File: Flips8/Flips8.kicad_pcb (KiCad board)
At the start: 2 copper layers, 100 x 100 mm, 24 parts, among them CN1 Conn_02x32_Row_Letter_First_A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, CN2 Conn_02x05_Odd_Even, U1 NCV7708, U2 NCV7708, U3 NCV7708, U4 NCV7708, U5 NCV7708, U6 NCV7708, U7 NCV7708, U8 74LS138

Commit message: proceed with Flips8
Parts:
- moved R1 5.08 mm to (83.8, 146.7), turned to 270 degrees
- moved R3 2.54 mm to (78.7, 146.7), turned to 270 degrees
- moved R2 2.54 mm to (81.3, 146.7), turned to 270 degrees
- moved C3 1.42 mm to (72.4, 127.6), turned to 90 degrees
- moved C2 1.42 mm to (63.5, 107.3), turned to 90 degrees
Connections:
- U3 pad 1: /X1 -> Net-(U3-Pad1)
- U3 pad 2: /X1 -> Net-(U3-Pad2)
- U3 pad 27: Net-(U3-Pad27) -> /X1
- U3 pad 28: Net-(U3-Pad28) -> /X1
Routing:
- net VCC: track 19.0 -> 142.4 mm, vias 1 -> 5
- net /X8: track 0.00 -> 92.7 mm
- net /X1: track 1.27 -> 92.0 mm
- net /X7: track 0.00 -> 87.6 mm
- net /X2: track 0.00 -> 87.4 mm
- net /X9: track 0.00 -> 81.3 mm
- net /X5: track 0.00 -> 80.4 mm
- net /X4: track 0.00 -> 77.2 mm
- net /X6: track 0.00 -> 76.8 mm
- net /X10: track 0.00 -> 76.8 mm
- net /X3: track 0.00 -> 74.7 mm
- net /SO: track 19.8 -> 94.5 mm, vias 1 -> 4
- net /EN: track 21.4 -> 95.8 mm, vias 1 -> 4
- net /~SY12: track 0.00 -> 73.3 mm
- net /X14: track 0.00 -> 69.5 mm
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
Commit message: finish initial routing of Flips8
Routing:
- net /SI: track 76.9 -> 282.1 mm, vias 3 -> 8
- net /SCLK: track 77.5 -> 280.7 mm, vias 3 -> 8
- net /SO: track 94.5 -> 294.0 mm, vias 4 -> 9
- net /EN: track 95.8 -> 286.3 mm, vias 4 -> 9
- net VCC: track 142.4 -> 281.4 mm, vias 5 -> 9
- net /~CS7: track 0.00 -> 133.0 mm, vias 0 -> 2
- net /~CS6: track 0.00 -> 117.4 mm, vias 0 -> 2
- net +12V: track 133.5 -> 240.8 mm, vias 6 -> 10
- net /~CS5: track 0.00 -> 101.1 mm, vias 0 -> 2
- net /~CS4: track 0.00 -> 38.6 mm, vias 0 -> 2
- net /~CS1: track 62.1 -> 61.0 mm
- net /~CS2: track 50.3 -> 49.5 mm
- net /CSA2: track 31.0 -> 30.3 mm

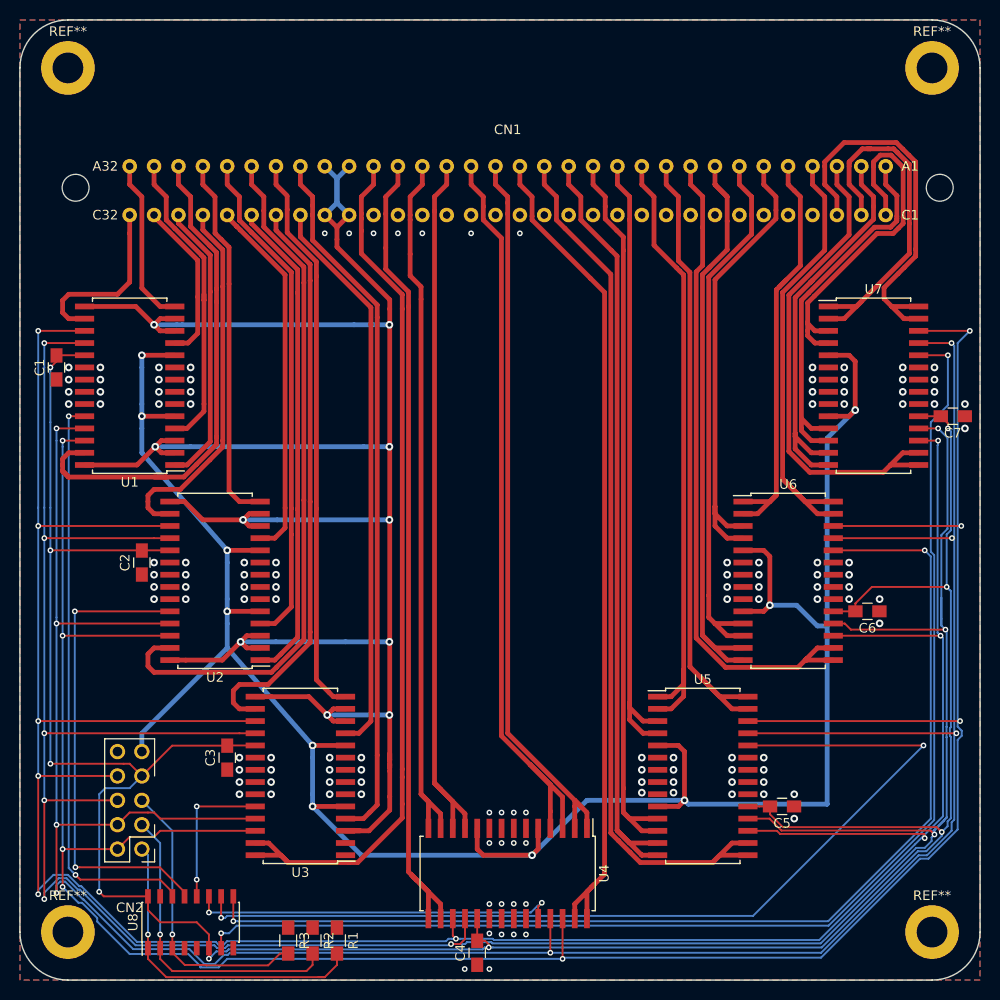
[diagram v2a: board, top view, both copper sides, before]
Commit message: more systematic tracing for Flisp8
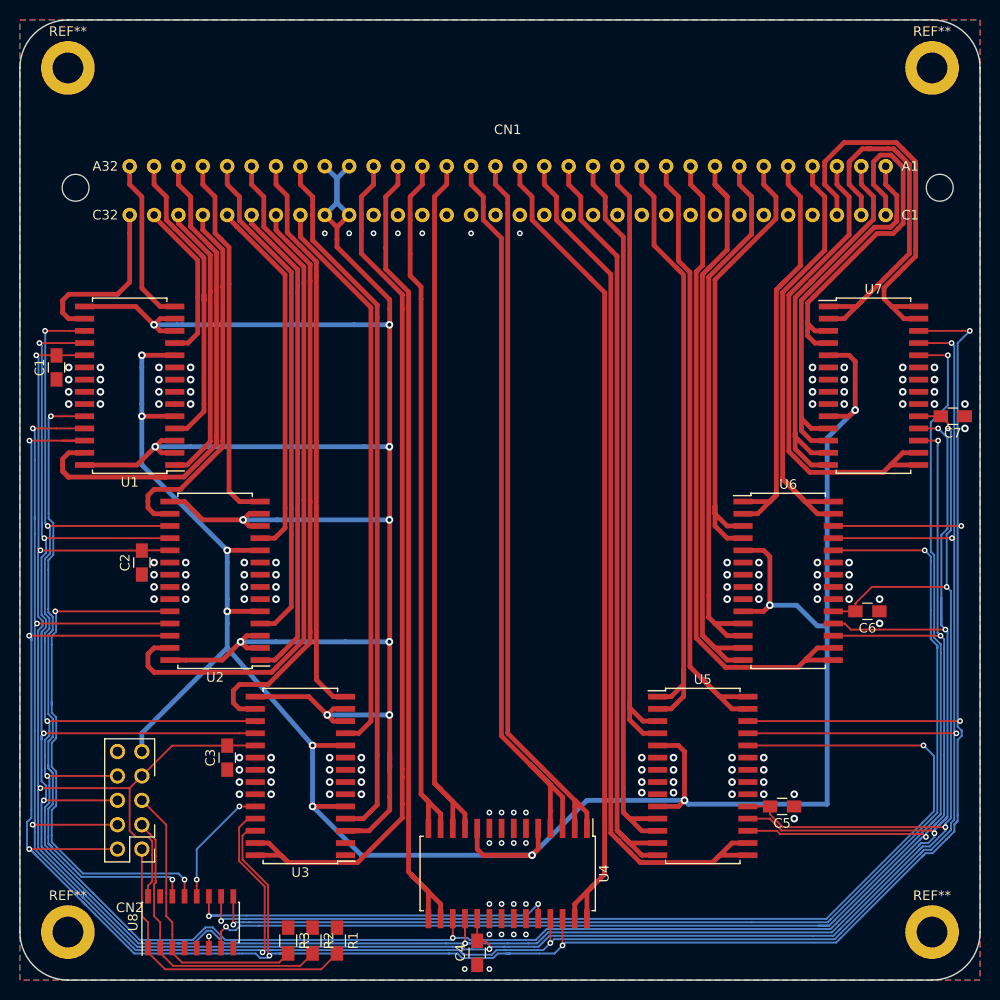
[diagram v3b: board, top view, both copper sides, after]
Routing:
- net VCC: track 281.4 -> 302.4 mm, vias 9 -> 8
- net /SI: track 282.1 -> 298.5 mm
- net /SCLK: track 280.7 -> 287.3 mm
- net /~CS1: track 61.0 -> 67.2 mm
- net /~CS5: track 101.1 -> 107.1 mm
- net /~CS2: track 49.5 -> 54.5 mm
- net /~CS7: track 133.0 -> 137.1 mm
- net /EN: track 286.3 -> 283.6 mm, vias 9 -> 8
- net /~CS3: track 15.5 -> 12.9 mm
- net /CSA0: track 34.5 -> 32.1 mm, vias 1 -> 0
- net /CSA1: track 32.6 -> 31.2 mm, vias 1 -> 0
- net /~CS6: track 117.4 -> 118.7 mm
- net /SO: track 294.0 -> 293.2 mm, vias 9 -> 8
- net /~CS4: track 38.6 -> 39.2 mm
- net /CSA2: track 30.3 -> 30.1 mm, vias 1 -> 0

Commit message: reposition ncv7708 of Flisp8
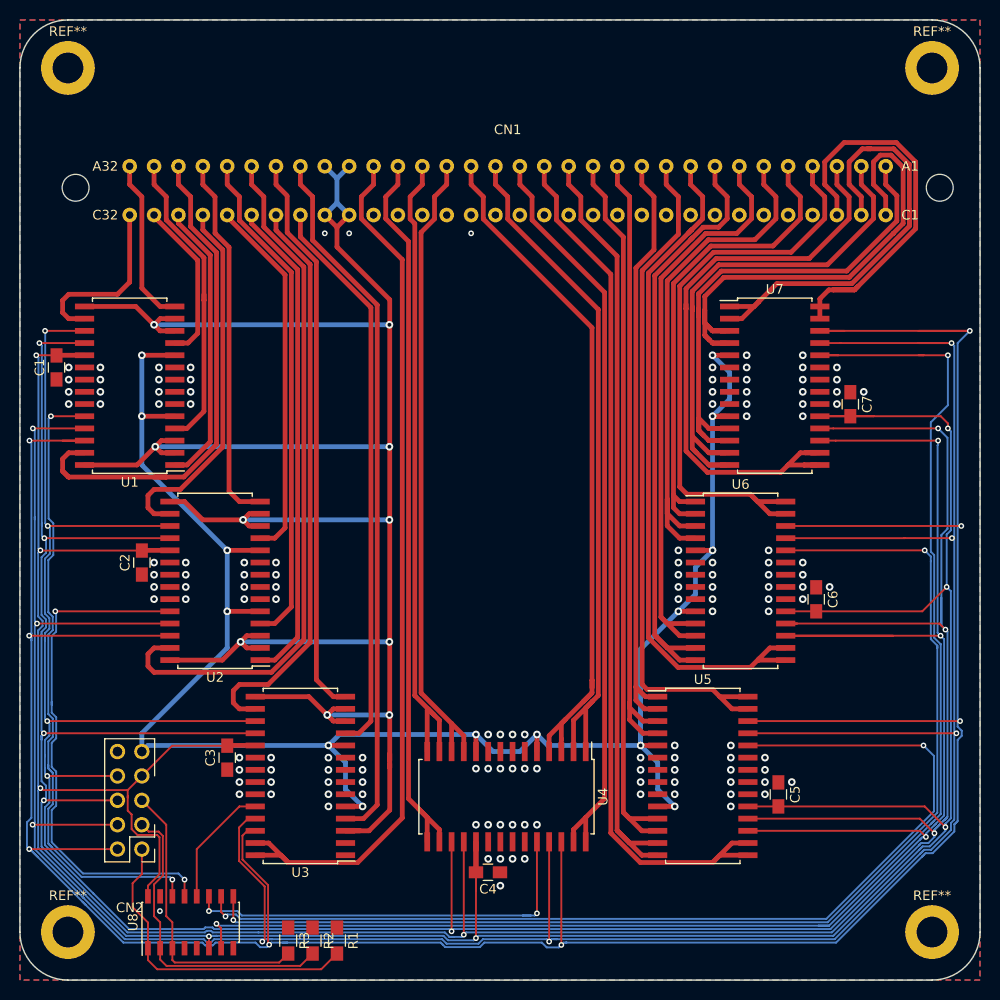
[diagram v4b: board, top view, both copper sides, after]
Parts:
- moved C7 10.7 mm to (137.3, 90.8), turned to 270 degrees
- moved U7 10.3 mm to (129.4, 88.9)
- moved C4 8.46 mm to (99.5, 139.6), turned to 180 degrees
- moved U4 8.00 mm to (101.5, 131.7)
- moved C6 5.48 mm to (133.7, 111.1), turned to 270 degrees
- moved U6 4.95 mm to (125.9, 109.2)
- moved C5 1.31 mm to (129.8, 131.5), turned to 270 degrees
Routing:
- net +12V: track 241.2 -> 202.0 mm, vias 10 -> 14
- net VCC: track 302.4 -> 334.5 mm
- net /EN: track 283.6 -> 313.1 mm
- net /SI: track 298.5 -> 327.5 mm
- net /SCLK: track 287.3 -> 312.5 mm
- net /SO: track 293.2 -> 314.6 mm
- net /X22: track 39.6 -> 57.7 mm
- net /X23: track 37.7 -> 55.4 mm
- net /X21: track 42.3 -> 57.9 mm
- net /X20: track 51.0 -> 64.8 mm
- net /X19: track 47.9 -> 61.1 mm
- net /~CS7: track 137.1 -> 150.0 mm
- net /X2: track 87.4 -> 77.0 mm
- net /X4: track 77.2 -> 66.8 mm
- net /X7: track 87.6 -> 77.9 mm
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
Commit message: more cleanup on pcb
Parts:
- moved U1 6.86 mm to (69.1, 88.9)
- moved C1 6.60 mm to (61.2, 87.1)
- moved U2 4.83 mm to (75.9, 109.2)
- moved C2 4.57 mm to (68.1, 107.3)
- moved C3 0.25 mm to (72.1, 127.6)
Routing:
- net /RY: track 234.1 -> 202.6 mm
- net /SCLK: track 312.5 -> 331.6 mm
- net /SO: track 314.6 -> 330.4 mm
- net /EN: track 313.1 -> 324.9 mm
- net VCC: track 334.5 -> 345.9 mm
- net /~SY13: track 59.9 -> 71.2 mm
- net /~SY7: track 38.7 -> 49.6 mm
- net /X23: track 55.4 -> 46.3 mm
- net /X22: track 57.7 -> 49.5 mm
- net +12V: track 202.0 -> 193.9 mm
- net /X21: track 57.9 -> 50.1 mm
- net /~CS1: track 67.2 -> 74.8 mm
- net /SI: track 327.5 -> 334.5 mm
- net /~SY1: track 18.6 -> 12.4 mm
- net /~CS2: track 54.5 -> 60.1 mm
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
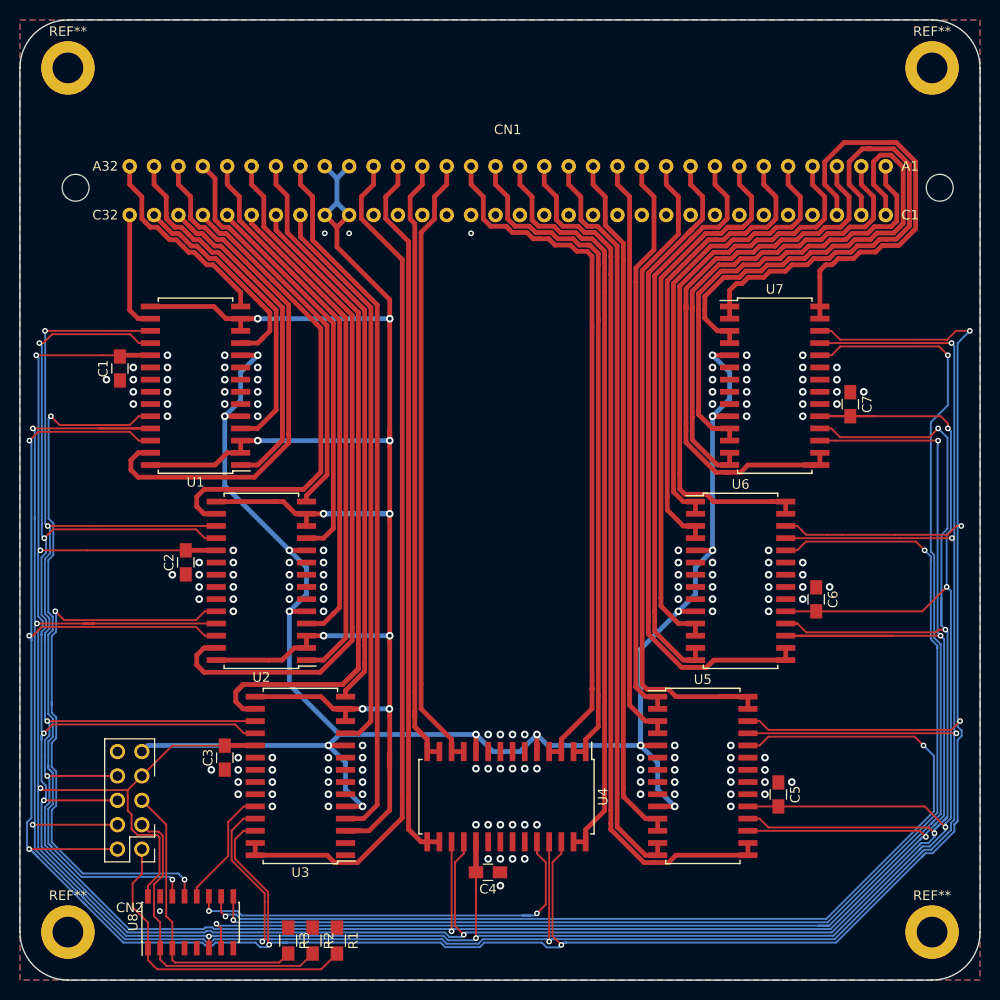
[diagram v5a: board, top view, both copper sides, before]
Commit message: rearrange connector and decoder; move 'bus' away from board edge pt. 1
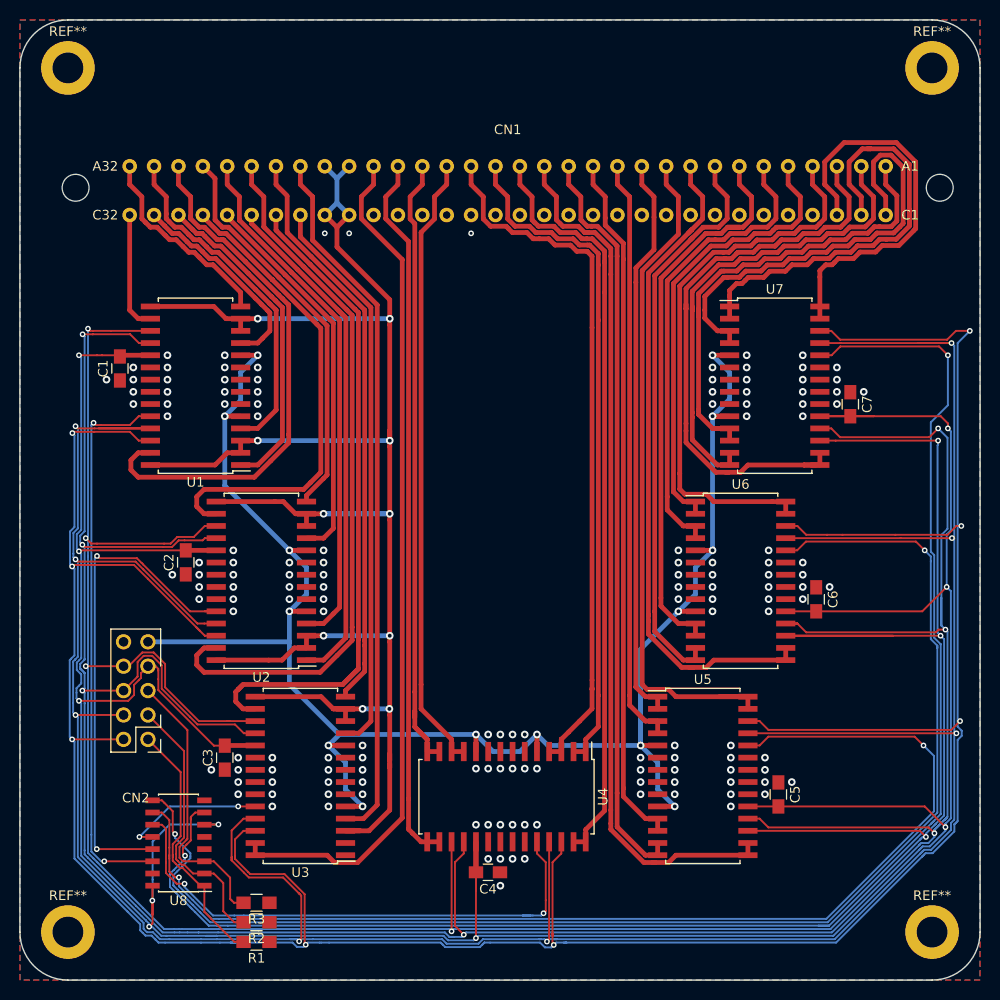
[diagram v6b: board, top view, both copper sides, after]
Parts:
- moved CN2 11.4 mm to (64.1, 125.7)
- moved R1 8.38 mm to (75.4, 146.8), turned to 180 degrees
- moved U8 8.35 mm to (67.3, 136.5), turned to 180 degrees
- moved R2 6.14 mm to (75.4, 144.8), turned to 180 degrees
- moved R3 5.14 mm to (75.4, 142.7), turned to 180 degrees
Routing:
- net /EN: track 324.9 -> 304.1 mm, vias 8 -> 7
- net /SO: track 330.4 -> 311.9 mm, vias 8 -> 7
- net /~CS6: track 123.9 -> 141.4 mm
- net /~CS1: track 74.8 -> 57.9 mm
- net /~CS5: track 107.3 -> 120.7 mm
- net /~CS7: track 149.2 -> 161.6 mm
- net /~CS4: track 45.0 -> 56.4 mm
- net /SI: track 334.5 -> 323.8 mm
- net /SCLK: track 331.6 -> 322.4 mm
- net /~CS2: track 60.1 -> 52.5 mm
- net /CSA0: track 33.4 -> 26.9 mm
- net VCC: track 345.9 -> 340.6 mm, vias 8 -> 10
- net +12V: track 193.9 -> 189.0 mm
- net /CSA1: track 32.9 -> 28.4 mm
- net /~CS3: track 12.6 -> 14.7 mm, vias 0 -> 2
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
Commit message: fixing supply connection between ICs and capacitors
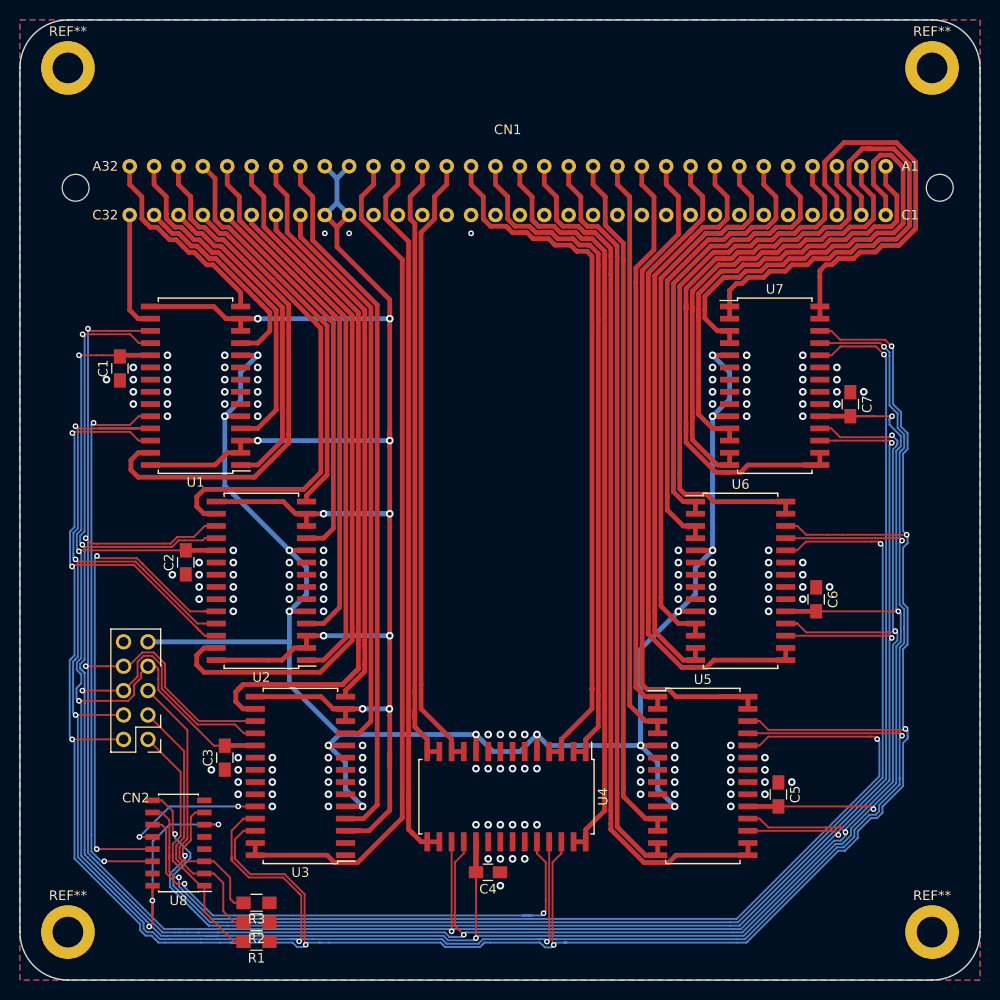
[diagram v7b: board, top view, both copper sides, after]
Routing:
- net /EN: track 304.1 -> 265.8 mm
- net /SO: track 311.9 -> 277.8 mm
- net /SI: track 323.8 -> 294.3 mm
- net /SCLK: track 322.4 -> 294.7 mm
- net VCC: track 340.6 -> 313.6 mm
- net /~CS7: track 161.6 -> 144.6 mm
- net /~CS6: track 141.4 -> 128.7 mm
- net /~CS5: track 120.7 -> 108.0 mm

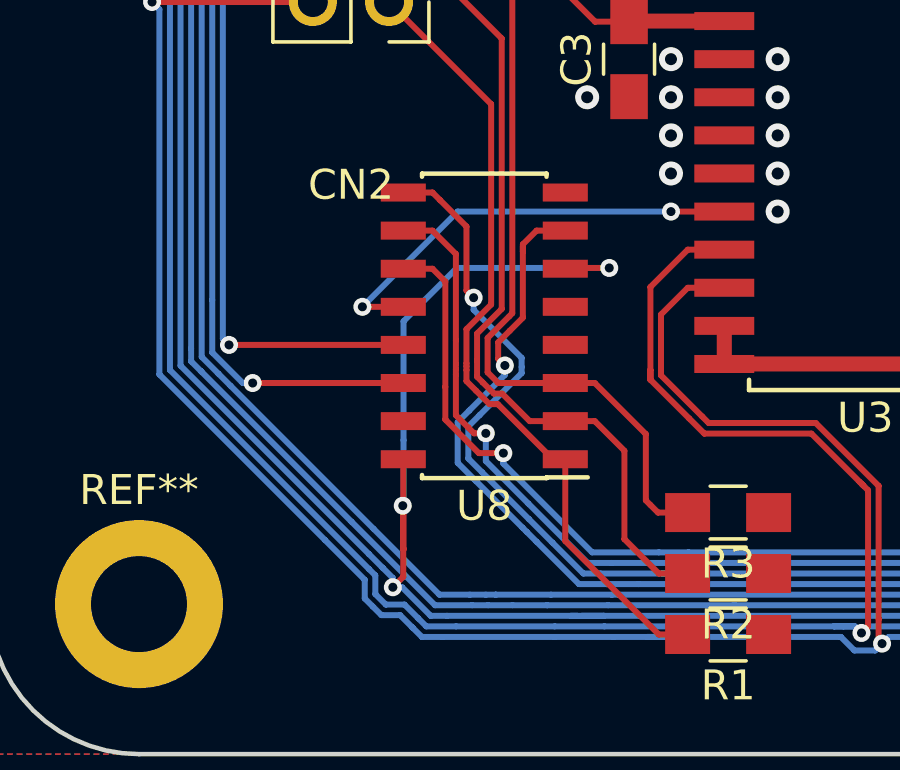
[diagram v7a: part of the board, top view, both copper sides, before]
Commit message: adding bypass capacitor for decoder in flips
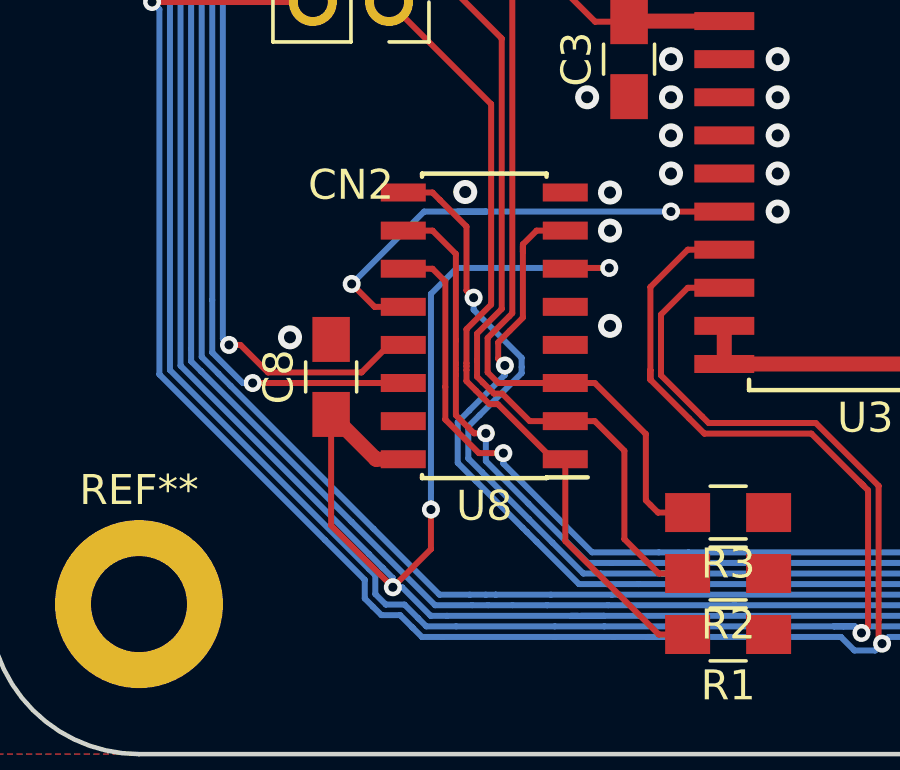
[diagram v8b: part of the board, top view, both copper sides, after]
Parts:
- added C8: 0μ1, Capacitors_SMD:C_0805_HandSoldering, F.Cu at (62.2, 138.2)
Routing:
- net VCC: track 313.6 -> 320.2 mm
- net /~CS3: track 14.7 -> 16.4 mm
- net /~CS2: track 52.5 -> 53.3 mm
- net GND: vias 148 -> 153
